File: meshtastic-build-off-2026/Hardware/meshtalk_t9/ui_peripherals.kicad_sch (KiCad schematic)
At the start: 24 parts, among them SW10 SW_Push, SW11 SW_Push, SW12 SW_Push, SW13 SW_Push, SW14 SW_Push, SW15 SW_Push, SW16 SW_Push, SW17 SW_Push, SW2 SW_Push, SW3 SW_Push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

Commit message: Replace AP2112K-3.3  with AP7361C-33E Connected LORA RF_SW1 to GPIO Added ESD Added mounting holes for display (Waveshare 2 inch) Added Boot and Reset buttons made power rails thicker added dedicated layer for 3v3 and GND
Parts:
- SW10, SW11, SW12, SW13, SW14, SW15, SW16, SW17, SW2, SW3, SW4, SW5, SW6, SW7, SW8, SW9: MPN (none) -> B3FS-1002P; Manufacturer (none) -> Omron
- TP1, TP2, TP3, TP4, TP5, TP6, TP7, TP8: now left out of the parts list

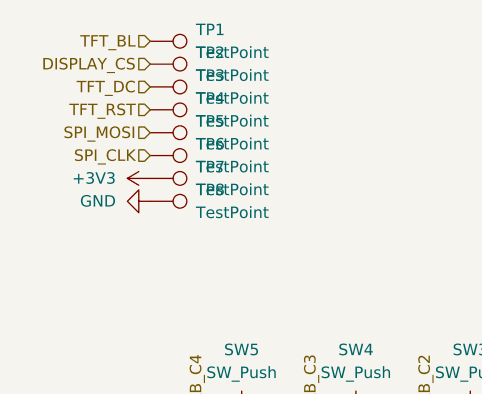
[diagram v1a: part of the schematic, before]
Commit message: PCB Updates - Align net names Clearence for esp32 antenna
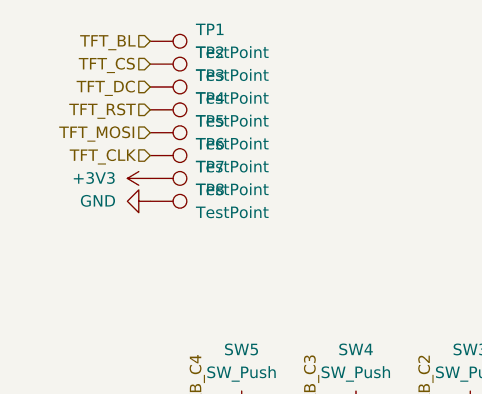
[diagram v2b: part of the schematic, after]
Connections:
- net DISPLAY_CS renamed TFT_CS
- net SPI_CLK renamed TFT_CLK
- net SPI_MOSI renamed TFT_MOSI
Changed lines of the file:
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@@
 		)
 	)
-	(hierarchical_label "SPI_MOSI"
+	(hierarchical_label "TFT_MOSI"
 		(shape input)
 		(at 73.66 60.96 180)
@@
 		)
 	)
-	(hierarchical_label "SPI_CLK"
+	(hierarchical_label "TFT_CLK"
 		(shape input)
 		(at 73.66 63.5 180)
@@
 		)
 	)
-	(hierarchical_label "DISPLAY_CS"
+	(hierarchical_label "TFT_CS"
 		(shape input)
 		(at 73.66 53.34 180)
